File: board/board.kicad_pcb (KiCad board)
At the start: 4 copper layers, 29 x 29 mm, 32 parts, among them J1 001_I2C, J2 011_GPIO, Q1 Q_PMOS_DGS, Q2 Q_NMOS_DGS, U1 ALED7709ATR

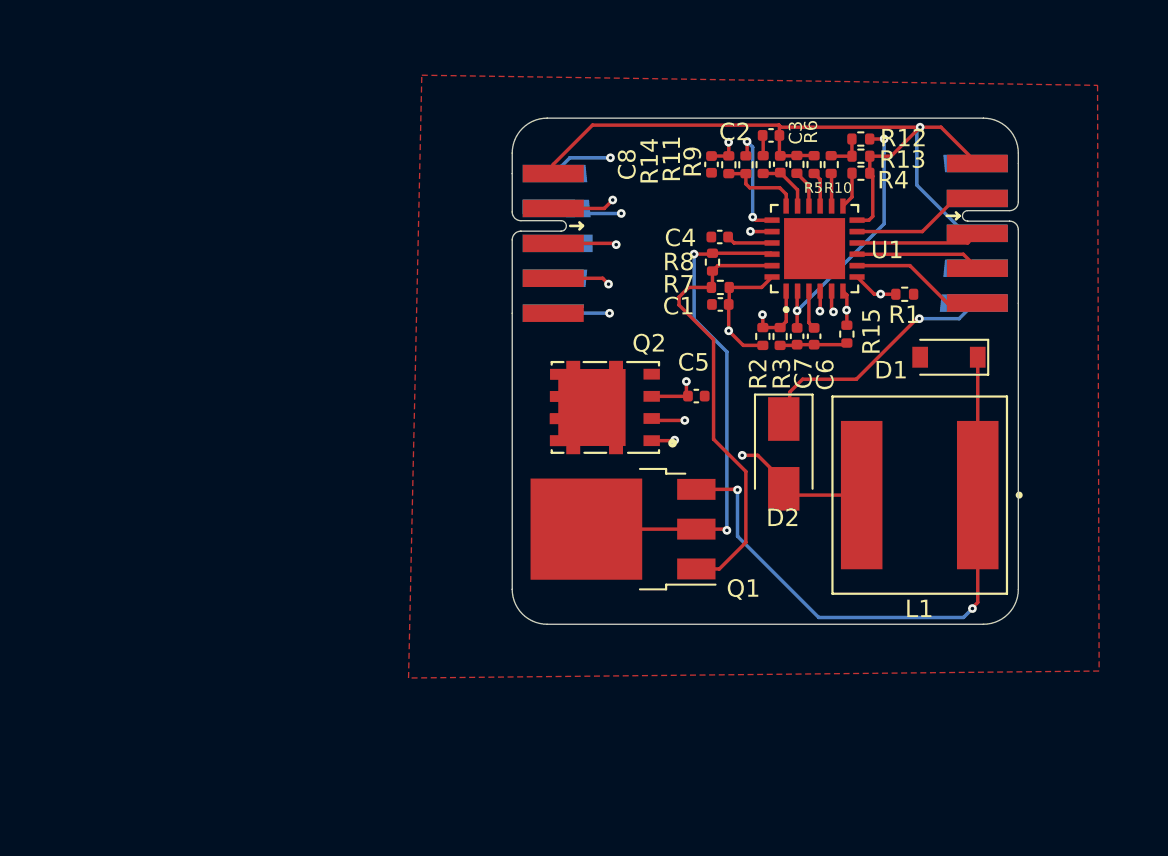
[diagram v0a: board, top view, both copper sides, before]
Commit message: Add Testpoint | Add relative footrpint/symbol path
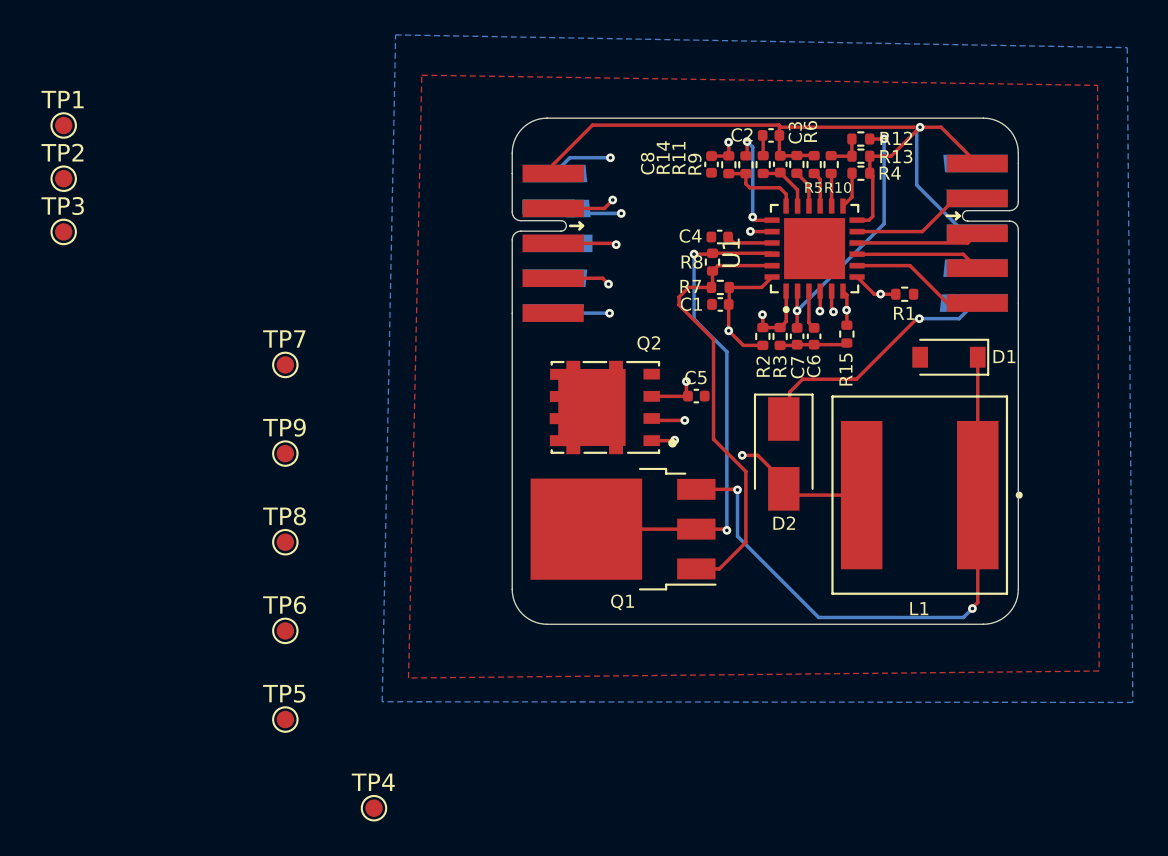
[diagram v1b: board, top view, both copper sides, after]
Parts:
- added TP1: TestPoint, TestPoint:TestPoint_Pad_D1.0mm, F.Cu at (114.3, 90.4)
- added TP2: TestPoint, TestPoint:TestPoint_Pad_D1.0mm, F.Cu at (114.3, 93.5)
- added TP3: TestPoint, TestPoint:TestPoint_Pad_D1.0mm, F.Cu at (114.3, 96.5)
- added TP4: TestPoint, TestPoint:TestPoint_Pad_D1.0mm, F.Cu at (132.1, 129.5)
- added TP5: TestPoint, TestPoint:TestPoint_Pad_D1.0mm, F.Cu at (127.0, 124.5)
- added TP6: TestPoint, TestPoint:TestPoint_Pad_D1.0mm, F.Cu at (127.0, 119.4)
- added TP7: TestPoint, TestPoint:TestPoint_Pad_D1.0mm, F.Cu at (127.0, 104.1)
- added TP8: TestPoint, TestPoint:TestPoint_Pad_D1.0mm, F.Cu at (127.0, 114.3)
- added TP9: TestPoint, TestPoint:TestPoint_Pad_D1.0mm, F.Cu at (127.0, 109.2)
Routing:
- added copper zone on B.Cu, net GND
- added copper zone on In1.Cu, net GND
- added copper zone on In2.Cu, net GND
